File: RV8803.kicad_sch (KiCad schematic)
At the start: 10 parts, among them IC901 RV-8803-C7-32.768k-3PPM-TA-QA

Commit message: Start of layout
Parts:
- C901: MPN (none) -> FC0H224ZFTBR24; Manufacturer (none) -> KEMET
- C902: footprint Capacitor_SMD:C_0603_1608Metric -> Capacitor_SMD:C_0402_1005Metric
- D901: MPN (none) -> BAS70L,315
- IC901: MPN (none) -> RV-8803-C7-32.768k-3PPM-TA-QA
- R901: MPN CRCW060347K5FKEAC -> RC0603JR-07330RL
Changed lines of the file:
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@@
       (effects (font (size 1.27 1.27)) hide)
     )
-    (property "Description" "47.5 kOhms ±1% 0.1W, 1/10W Chip Resistor 0603" (id 13) (at 194.31 80.01 0)
+    (property "Description" "100 kOhms ±1% 0.1W, 1/10W Chip Resistor 0603" (id 13) (at 194.31 80.01 0)
       (effects (font (size 1.27 1.27)) hide)
     )
@@
       (effects (font (size 1.27 1.27)) (justify left))
     )
-    (property "Footprint" "Capacitor_SMD:C_0603_1608Metric" (id 2) (at 129.54 99.06 0)
+    (property "Footprint" "Capacitor_SMD:C_0402_1005Metric" (id 2) (at 129.54 99.06 0)
       (effects (font (size 1.27 1.27)) hide)
     )
@@
       (effects (font (size 1.27 1.27)) (justify left) hide)
     )
+    (property "MPN" "FC0H224ZFTBR24" (id 10) (at 101.6 104.14 0)
+      (effects (font (size 1.27 1.27)) hide)
+    )
+    (property "Manufacturer" "KEMET" (id 11) (at 101.6 104.14 0)
+      (effects (font (size 1.27 1.27)) hide)
+    )
     (pin "1")
     (pin "2")
@@
       (effects (font (size 1.27 1.27)) hide)
     )
-    (property "Description" "47.5 kOhms ±1% 0.1W, 1/10W Chip Resistor 0603" (id 13) (at 185.42 80.01 0)
+    (property "Description" "100 kOhms ±1% 0.1W, 1/10W Chip Resistor 0603" (id 13) (at 185.42 80.01 0)
       (effects (font (size 1.27 1.27)) hide)
     )
@@
       (effects (font (size 1.27 1.27)) hide)
     )
-    (property "MPN" "CRCW060347K5FKEAC" (id 6) (at 101.6 99.06 0)
+    (property "MPN" "RC0603JR-07330RL" (id 6) (at 101.6 99.06 0)
       (effects (font (size 1.27 1.27)) hide)
     )
@@
       (effects (font (size 1.27 1.27)) hide)
     )
-    (property "Description" "47.5 kOhms ±1% 0.1W, 1/10W Chip Resistor 0603" (id 13) (at 101.6 99.06 0)
+    (property "Description" "330 Ohms ±5% 0.1W, 1/10W Chip Resistor 0603 (1608 Metric) Moisture Resistant Thick Film" (id 13) (at 101.6 99.06 0)
       (effects (font (size 1.27 1.27)) hide)
     )
@@
     (property "Manufacturer_Part_Number" "BAS70L,315" (id 9) (at 119.38 72.39 0)
       (effects (font (size 1.27 1.27)) (justify left) hide)
+    )
+    (property "MPN" "BAS70L,315" (id 10) (at 101.6 83.82 0)
+      (effects (font (size 1.27 1.27)) hide)
     )
     (pin "1")
@@
     (property "Manufacturer_Part_Number" "RV-8803-C7-32.768k-3PPM-TA-QA" (id 9) (at 158.75 100.33 0)
       (effects (font (size 1.27 1.27)) (justify left) hide)
+    )
+    (property "MPN" "RV-8803-C7-32.768k-3PPM-TA-QA" (id 10) (at 132.08 85.09 0)
+      (effects (font (size 1.27 1.27)) hide)
     )
     (pin "1")
@@
       (effects (font (size 1.27 1.27)) hide)
     )
-    (property "Description" "47.5 kOhms ±1% 0.1W, 1/10W Chip Resistor 0603" (id 13) (at 110.49 77.47 0)
-      (effects (font (size 1.27 1.27)) hide)
-    )
+    (property "Description" "100 kOhms ±1% 0.1W, 1/10W Chip Resistor 0603" (id 13) (at 110.49 77.47 0)
+      (effects (font (size 1.27 1.27)) hide)
+    )

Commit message: updated new layout - no routing
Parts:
- C901: symbol SamacSys_Parts:FC0H224ZFTBR24 -> sapphireMini:FC0H224ZFTBR24
- D901: symbol SamacSys_Parts:BAS70L,315 -> sapphireMini:BAS70L,315
- IC901: symbol SamacSys_Parts:RV-8803-C7-32.768k-3PPM-TA-QA -> sapphireMini:RV-8803-C7-32.768k-3PPM-TA-QA
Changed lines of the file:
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@@
     (pin "2")
   )
-  (symbol (lib_id "SamacSys_Parts:FC0H224ZFTBR24") (at 101.6 104.14 270) (unit 1)
+  (symbol (lib_id "sapphireMini:FC0H224ZFTBR24") (at 101.6 104.14 270) (unit 1)
     (in_bom yes) (on_board yes)
     (property "Reference" "C901" (id 0) (at 104.902 113.4653 90)
@@
     (pin "2")
   )
-  (symbol (lib_id "SamacSys_Parts:BAS70L,315") (at 101.6 83.82 90) (unit 1)
+  (symbol (lib_id "sapphireMini:BAS70L,315") (at 101.6 83.82 90) (unit 1)
     (in_bom yes) (on_board yes)
     (property "Reference" "D901" (id 0) (at 95.25 76.2 90)
@@
     (pin "2")
   )
-  (symbol (lib_id "SamacSys_Parts:RV-8803-C7-32.768k-3PPM-TA-QA") (at 132.08 85.09 0) (unit 1)
+  (symbol (lib_id "sapphireMini:RV-8803-C7-32.768k-3PPM-TA-QA") (at 132.08 85.09 0) (unit 1)
     (in_bom yes) (on_board yes) (fields_autoplaced)
     (property "Reference" "IC901" (id 0) (at 147.32 78.901 0))

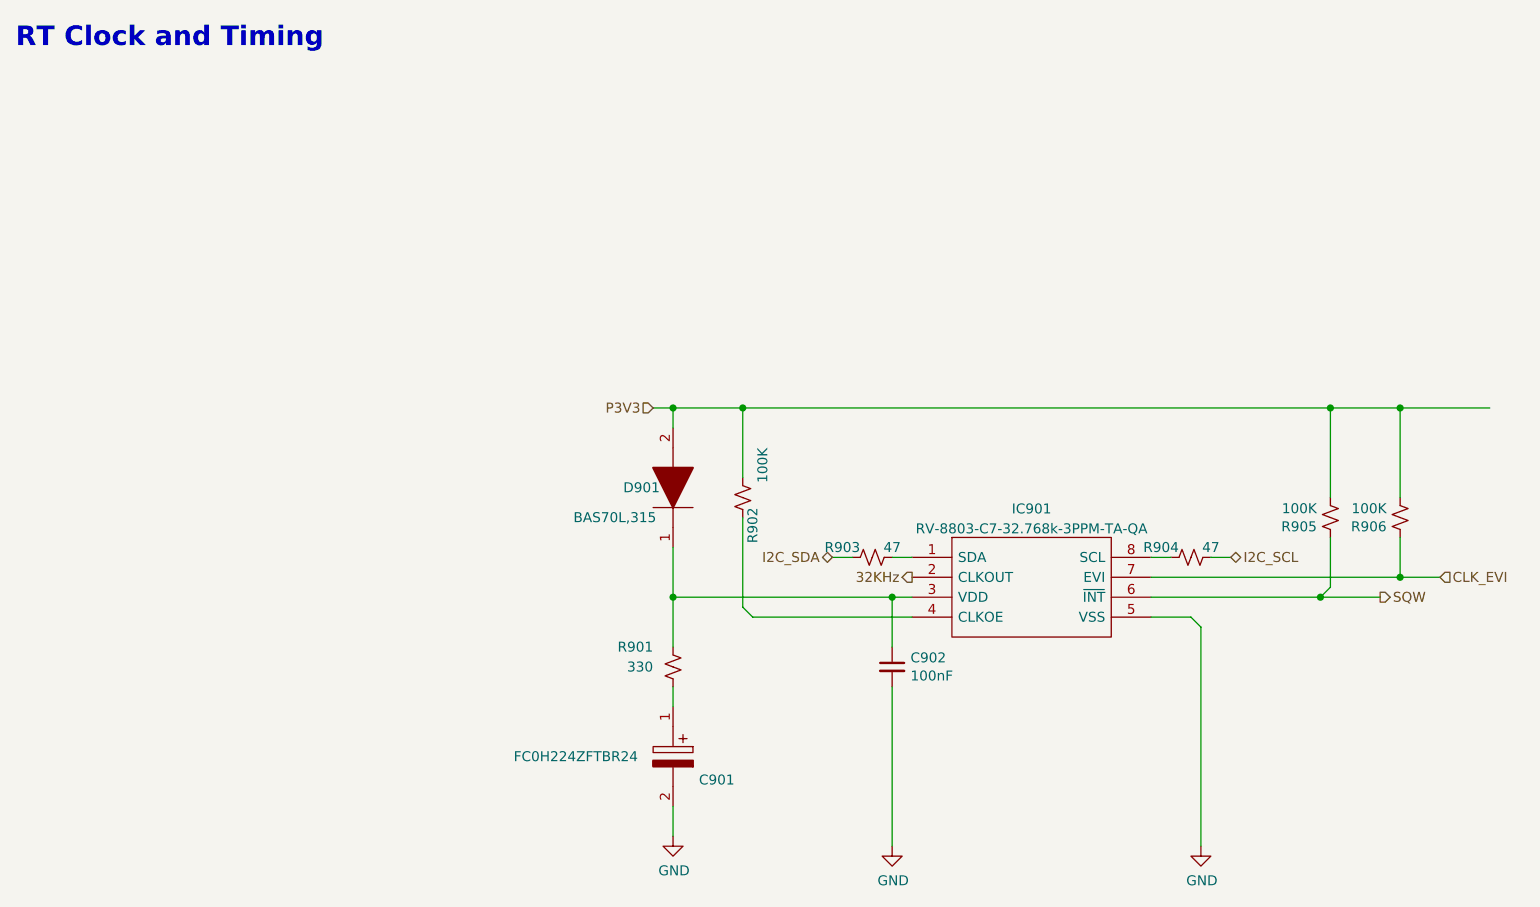
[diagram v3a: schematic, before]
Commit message: 6 Layer Routing
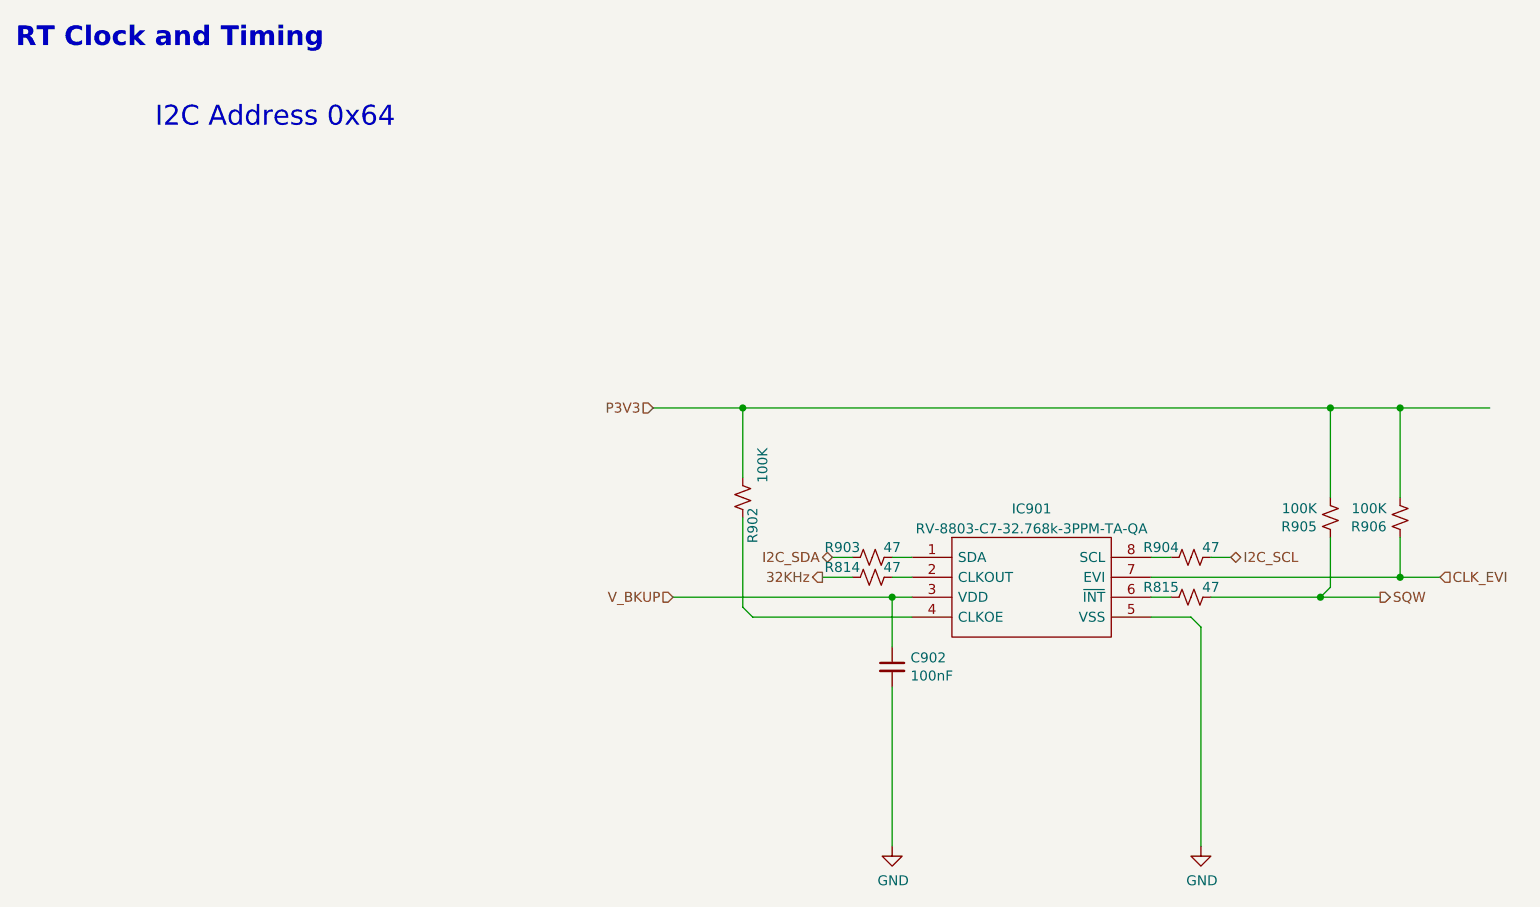
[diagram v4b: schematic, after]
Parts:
- removed C901: FC0H224ZFTBR24, CAPAE1080X880N, symbol sapphireMini:FC0H224ZFTBR24
- removed D901: BAS70L,315, PESD5V0S1BL315, symbol sapphireMini:BAS70L,315
- removed R901: 330, Resistor_SMD:R_0603_1608Metric, symbol Device:R_Small_US
- added R814, R815: 47, Resistor_SMD:R_0603_1608Metric, symbol Device:R_Small_US
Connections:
- net 32KHz: now also R814.2; no longer IC901.2 (CLKOUT)
- net SQW: now also R815.1; no longer IC901.6 (~{INT})
- net V_BKUP: now reaches C902.1, IC901.3 (VDD)
- new net: IC901.6 (~{INT}), R815.2
- new net: IC901.2 (CLKOUT), R814.1
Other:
- note added: "I2C Address 0x64"

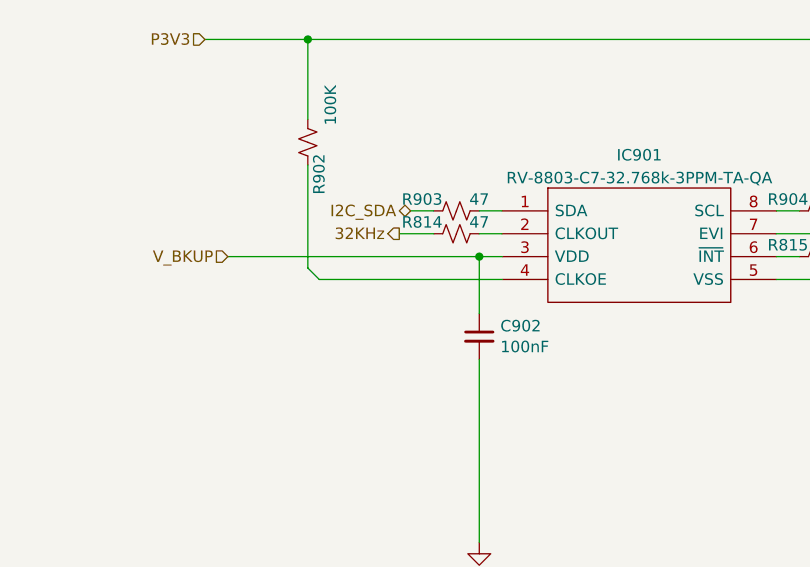
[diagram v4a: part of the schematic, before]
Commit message: Updated to fix noted problems
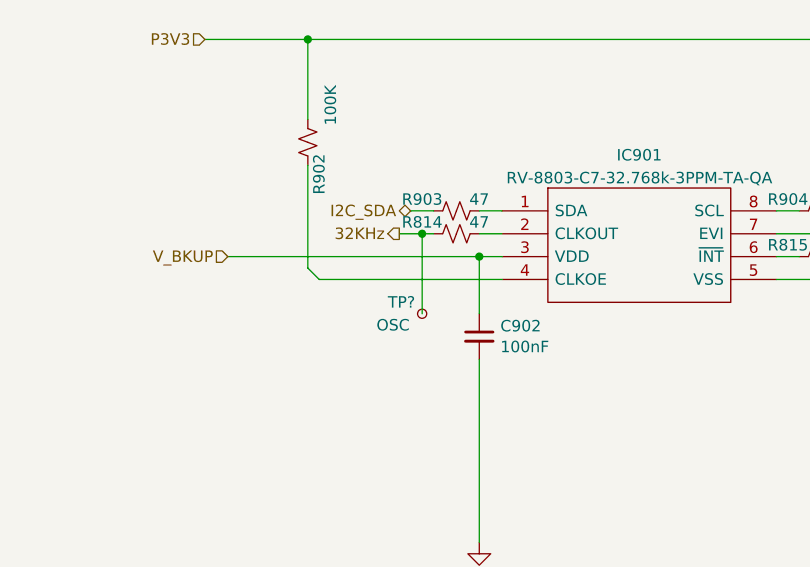
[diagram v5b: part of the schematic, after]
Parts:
- added TP?: OSC, TestPoint:TestPoint_Pad_D2.0mm, symbol Connector:TestPoint_Small
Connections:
- net 32KHz: now also TP?.1
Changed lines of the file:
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@@
   (junction (at 194.31 66.04) (diameter 0) (color 0 0 0 0)
   )
+  (junction (at 123.19 87.63) (diameter 0) (color 0 0 0 0)
+  )
   (junction (at 184.15 90.17) (diameter 0) (color 0 0 0 0)
   )
@@
     (stroke (width 0) (type default) (color 0 0 0 0))
   )
-  (wire (pts (xy 120.65 87.63) (xy 124.46 87.63))
+  (wire (pts (xy 120.65 87.63) (xy 123.19 87.63))
     (stroke (width 0) (type default) (color 0 0 0 0))
   )
@@
     (stroke (width 0) (type default) (color 0 0 0 0))
   )
+  (wire (pts (xy 123.19 96.52) (xy 123.19 87.63))
+    (stroke (width 0) (type default) (color 0 0 0 0))
+  )
   (wire (pts (xy 170.18 85.09) (xy 172.72 85.09))
+    (stroke (width 0) (type default) (color 0 0 0 0))
+  )
+  (wire (pts (xy 123.19 87.63) (xy 124.46 87.63))
     (stroke (width 0) (type default) (color 0 0 0 0))
   )
@@
     (pin "2")
   )
+  (symbol (lib_id "Connector:TestPoint_Small") (at 123.19 96.52 0) (unit 1)
+    (in_bom yes) (on_board yes)
+    (property "Reference" "TP?" (id 0) (at 119.38 95.25 0)
+      (effects (font (size 1.27 1.27)) (justify left))
+    )
+    (property "Value" "OSC" (id 1) (at 118.11 97.79 0)
+      (effects (font (size 1.27 1.27)) (justify left))
+    )
+    (property "Footprint" "TestPoint:TestPoint_Pad_D2.0mm" (id 2) (at 128.27 96.52 0)
+      (effects (font (size 1.27 1.27)) hide)
+    )
+    (property "Datasheet" "~" (id 3) (at 128.27 96.52 0)
+      (effects (font (size 1.27 1.27)) hide)
+    )
+    (pin "1")
+  )
   (symbol (lib_id "Device:R_Small_US") (at 185.42 80.01 180) (unit 1)

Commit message: InProgress
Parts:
- gave numbers to parts that had none: 1
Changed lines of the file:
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@@
   (symbol (lib_id "Connector:TestPoint_Small") (at 123.19 96.52 0) (unit 1)
     (in_bom yes) (on_board yes)
-    (property "Reference" "TP?" (id 0) (at 119.38 95.25 0)
+    (property "Reference" "TP801" (id 0) (at 119.38 95.25 0)
       (effects (font (size 1.27 1.27)) (justify left))
     )
